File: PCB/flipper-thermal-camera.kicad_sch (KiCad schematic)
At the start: 27 parts, among them IC1 VEML7700-TT, J1 Conn_01x08, J2 Conn_01x10, U1 MLX90640ESF-BAB-000-SP, U2 XC6206PxxxMR, U3 ICM-20948, U4 SHT31-DIS

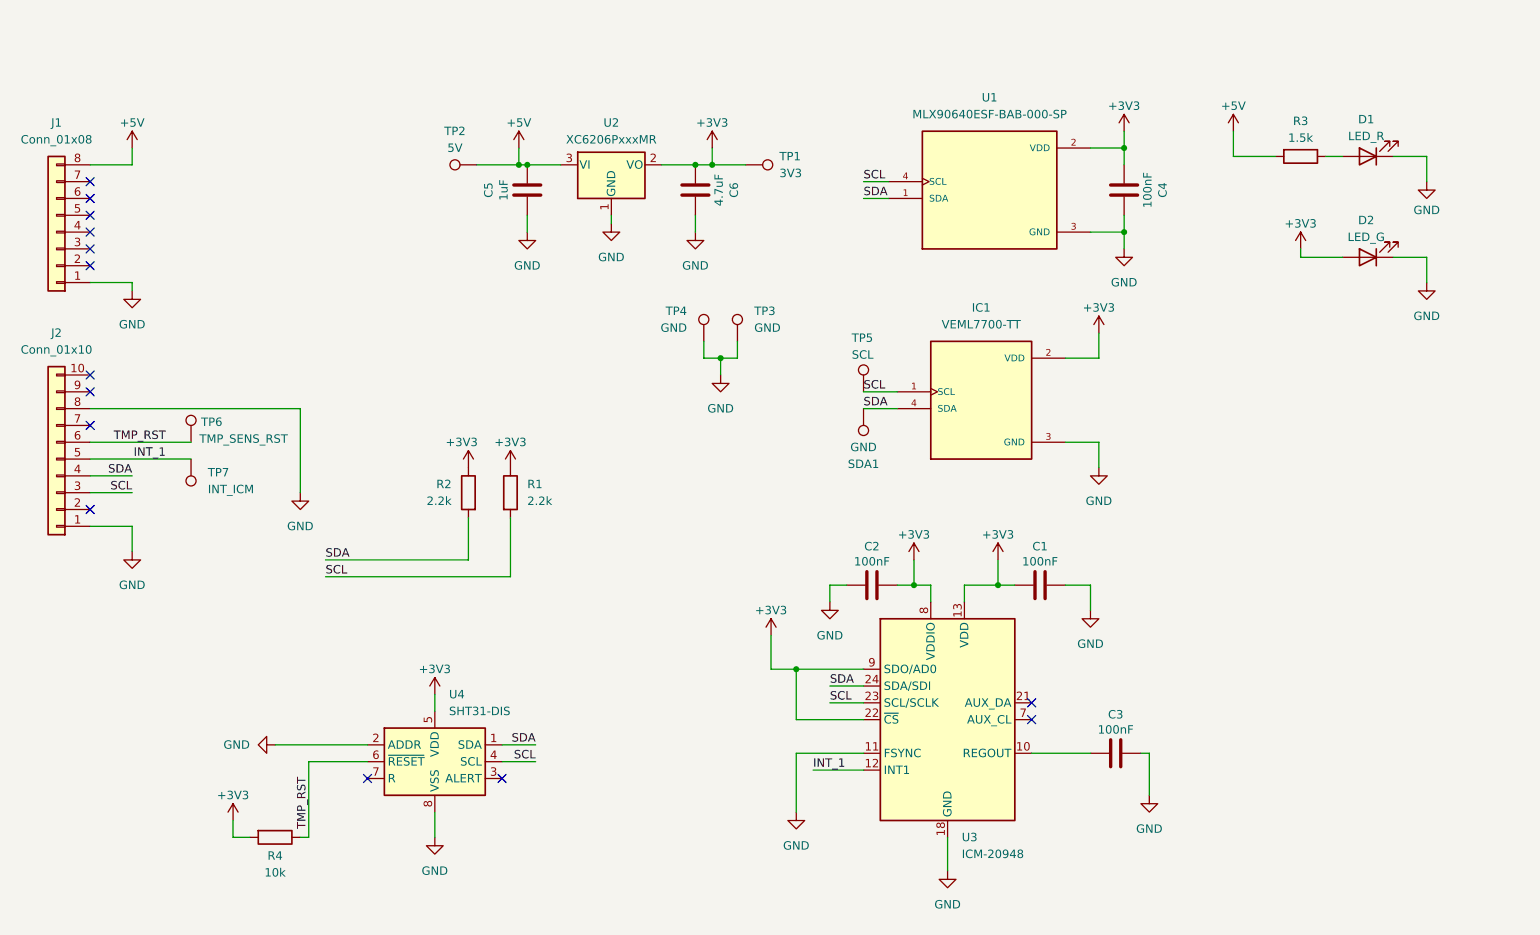
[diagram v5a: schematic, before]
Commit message: switch IMU and add more capacitors and diodes
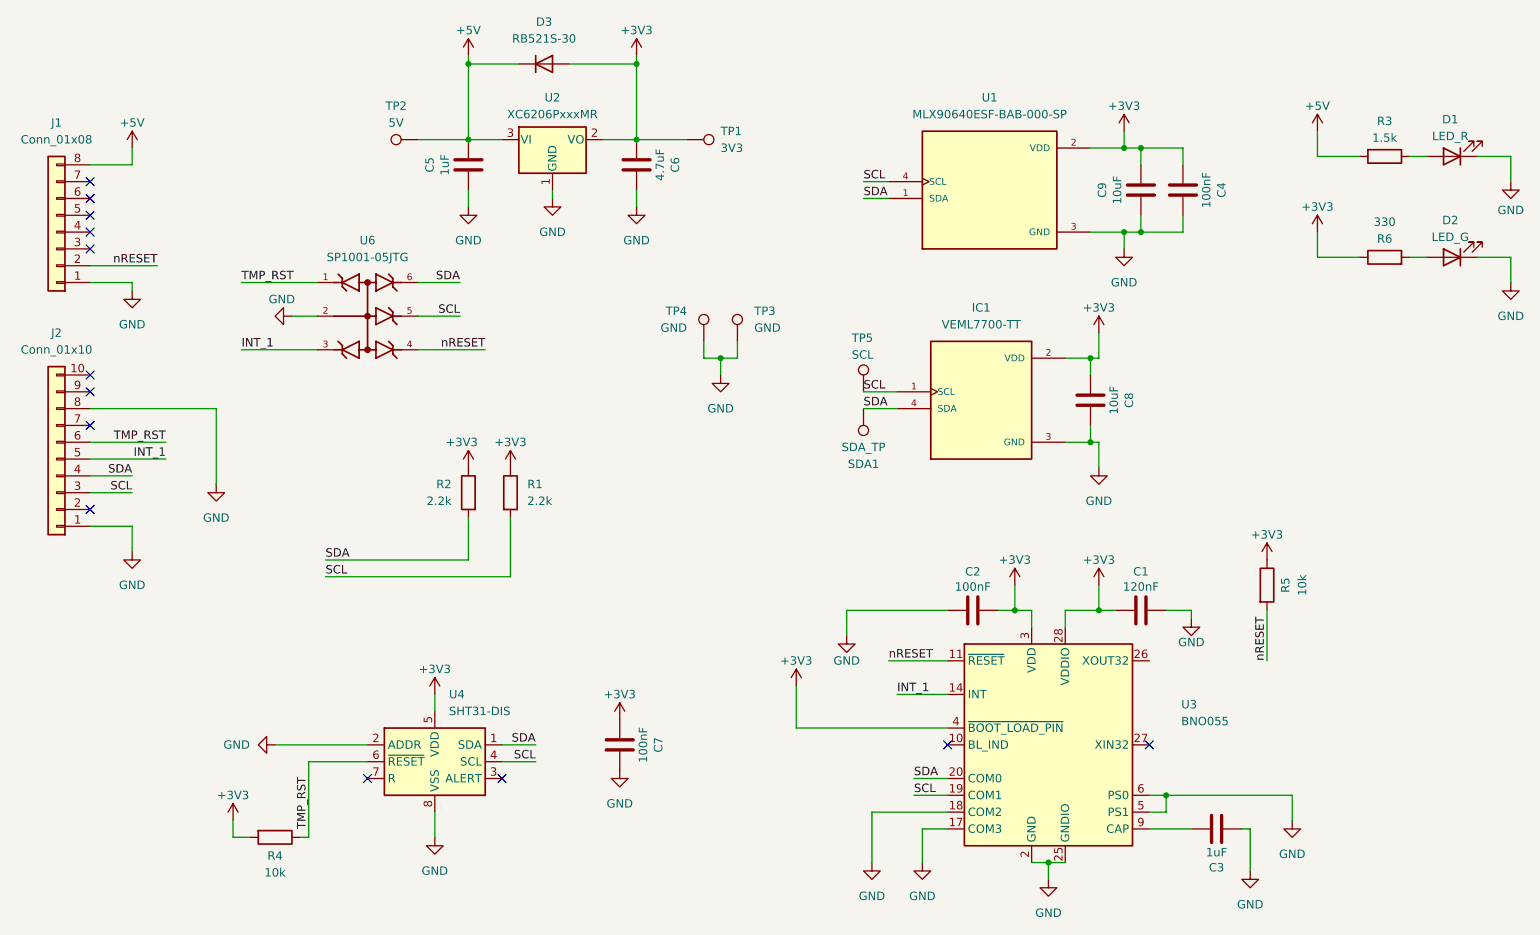
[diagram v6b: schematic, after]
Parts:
- removed TP6: TMP_SENS_RST, TestPoint:TestPoint_Pad_D2.0mm, symbol Connector:TestPoint
- removed TP7: INT_ICM, TestPoint:TestPoint_Pad_D2.0mm, symbol Connector:TestPoint
- removed U3: ICM-20948, Sensor_Motion:InvenSense_QFN-24_3x3mm_P0.4mm, symbol Sensor_Motion:ICM-20948
- added C7: 100nF, Capacitor_SMD:C_0805_2012Metric, symbol Device:C
- added C8, C9: 10uF, Capacitor_SMD:C_0805_2012Metric, symbol Device:C
- added D3: RB521S-30, Diode_SMD:D_SOD-523, symbol Device:D
- added R5: 10k, Resistor_SMD:R_0805_2012Metric, symbol Device:R
- added R6: 330, Resistor_SMD:R_0805_2012Metric, symbol Device:R
- added U3: BNO055, Package_LGA:LGA-28_5.2x3.8mm_P0.5mm, symbol Sensor_Motion:BNO055
- added U6: SP1001-05JTG, Components:SOP65P220X110-6N, symbol SP1001-05JTG:SP1001-05JTG
- C1: value 100nF -> 120nF
- C3: value 100nF -> 1uF
- SDA1: value GND -> SDA_TP
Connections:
- net +3V3: now also C7.1, C8.1, C9.1, D3.2 (A), R5.1, R6.1, U3.28 (VDDIO), U3.3 (VDD), U3.4 (~{BOOT_LOAD_PIN}); no longer D2.2 (A)
- net +5V: now also D3.1 (K)
- net GND: now also C3.1, C7.2, C8.2, C9.2, U3.17 (COM3), U3.18 (COM2), U3.2 (GND), U3.25 (GNDIO), U3.5 (PS1), U3.6 (PS0), U6.2; no longer C3.2
- net INT_1: now also U3.14 (INT), U6.3
- net SCL: now also U3.19 (COM1), U6.5
- net SDA: now also U3.20 (COM0), U6.6
- net TMP_RST: now also U6.1
- net nRESET: now reaches J1.2 (Pin_2)
- net nRESET: now also R5.2, U3.11 (~{RESET}), U6.4
- new net: C3.2, U3.9 (CAP)
- new net: D2.2 (A), R6.2
- no-connect marks 14 -> 13
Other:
- moved on the sheet: C4, C5, C6, D1, D2, R3, TP1, TP2, U2

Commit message: fix up wiring
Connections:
- net GND: now also U4.7 (R)
- no-connect marks 13 -> 12
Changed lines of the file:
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@@
-	)
-	(no_connect
-		(at 68.58 135.89)
 	)
 	(no_connect
@@
 	(wire
 		(pts
+			(xy 66.04 140.97) (xy 66.04 135.89)
+		)
+		(stroke
+			(width 0)
+			(type default)
+		)
+	)
+	(wire
+		(pts
 			(xy 121.92 72.39) (xy 121.92 74.93)
 		)
@@
 		(pts
 			(xy 68.58 130.81) (xy 54.61 130.81)
+		)
+		(stroke
+			(width 0)
+			(type default)
+		)
+	)
+	(wire
+		(pts
+			(xy 66.04 135.89) (xy 68.58 135.89)
 		)
 		(stroke
@@
 					(unit 1)
 				)
+			)
+		)
+	)
+	(symbol
+		(lib_id "power:GND")
+		(at 66.04 140.97 0)
+		(unit 1)
+		(body_style 1)
+		(exclude_from_sim no)
+		(in_bom yes)
+		(on_board yes)
+		(in_pos_files yes)
+		(dnp no)
+		(fields_autoplaced yes)
+		(property "Reference" "#PWR041"
+			(at 66.04 147.32 0)
+			(hide yes)
+			(show_name no)
+			(do_not_autoplace no)
+			(effects
+				(font
+					(size 1.27 1.27)
+				)
+			)
+		)
+		(property "Value" "GND"
+			(at 66.04 146.05 0)
+			(show_name no)
+			(do_not_autoplace no)
+			(effects
+				(font
+					(size 1.27 1.27)
+				)
+			)
+		)
+		(property "Footprint" ""
+			(at 66.04 140.97 0)
+			(hide yes)
+			(show_name no)
+			(do_not_autoplace no)
+			(effects
+				(font
+					(size 1.27 1.27)
+				)
+			)
+		)
+		(property "Datasheet" ""
+			(at 66.04 140.97 0)
+			(hide yes)
+			(show_name no)
+			(do_not_autoplace no)
+			(effects
+				(font
+					(size 1.27 1.27)
+				)
+			)
+		)
+		(property "Description" "Power symbol creates a global label with name \"GND\" , ground"
+			(at 66.04 140.97 0)
+			(hide yes)
+			(show_name no)
+			(do_not_autoplace no)
+			(effects
+				(font
+					(size 1.27 1.27)
+				)
+			)
+		)
+		(pin "1"
+		)
+		(instances
+			(project "flipper-thermal-camera"
+				(path "/20fef62b-baec-4471-9252-b8b8b3debd81"
+					(reference "#PWR041")
+					(unit 1)
+				)
